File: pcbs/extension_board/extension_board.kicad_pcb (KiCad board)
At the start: 4 copper layers, 100 x 82.5 mm, 502 parts, among them J1 Conn_02x32_Counter_Clockwise, J2 Conn_02x03_Odd_Even, J3 Conn_01x05, J4 Conn_02x05_Odd_Even, J5 Barrel_Jack, J6 Conn_02x19_Odd_Even, J7 Conn_02x19_Odd_Even, J8 Conn_01x08, Q1 MBT3904DW1, Q10 MBT3904DW1, Q11 MBT3904DW1, Q12 MBT3904DW1, Q13 MBT3904DW1, Q14 MBT3904DW1, Q15 MBT3904DW1, Q16 MBT3904DW1, Q17 MBT3904DW1, Q18 MBT3904DW1, Q19 MBT3904DW1, Q2 MBT3904DW1, Q20 MBT3904DW1, Q21 MBT3904DW1, Q22 MBT3904DW1, Q23 MBT3904DW1, Q24 MBT3904DW1, Q25 MBT3904DW1, Q26 MBT3904DW1, Q27 MBT3904DW1, Q28 MBT3904DW1, Q29 MBT3904DW1, Q3 MBT3904DW1, Q30 MBT3904DW1, Q31 MBT3904DW1, Q32 MBT3904DW1, Q4 MBT3904DW1, Q5 MBT3904DW1, Q6 MBT3904DW1, Q7 MBT3904DW1, Q8 MBT3904DW1, Q9 MBT3904DW1, SW1 MY_SW_Push_Dual, SW2 Rotary_Encoder, SW3 Rotary_Encoder, U1 LM324QT, U10 LM324QT, U11 LM324QT, U12 LM324QT, U13 LM324QT, U14 LM324QT, U15 LM324QT, U16 LM324QT, U17 LM324QT, U18 LM324QT, U19 LM324QT, U2 LM324QT, U20 LM324QT, U21 LM324QT, U22 LM324QT, U23 LM324QT, U24 LM324QT, U25 LM324QT, U26 LM324QT, U27 LM324QT, U28 LM324QT, U29 LM324QT, U3 LM324QT, U30 LM324QT, U31 LM324QT, U32 LM324QT, U33 DAC101C085, U34 TS30011/12/13, U4 LM324QT, U5 LM324QT, U6 LM324QT, U7 LM324QT, U8 LM324QT, U9 LM324QT

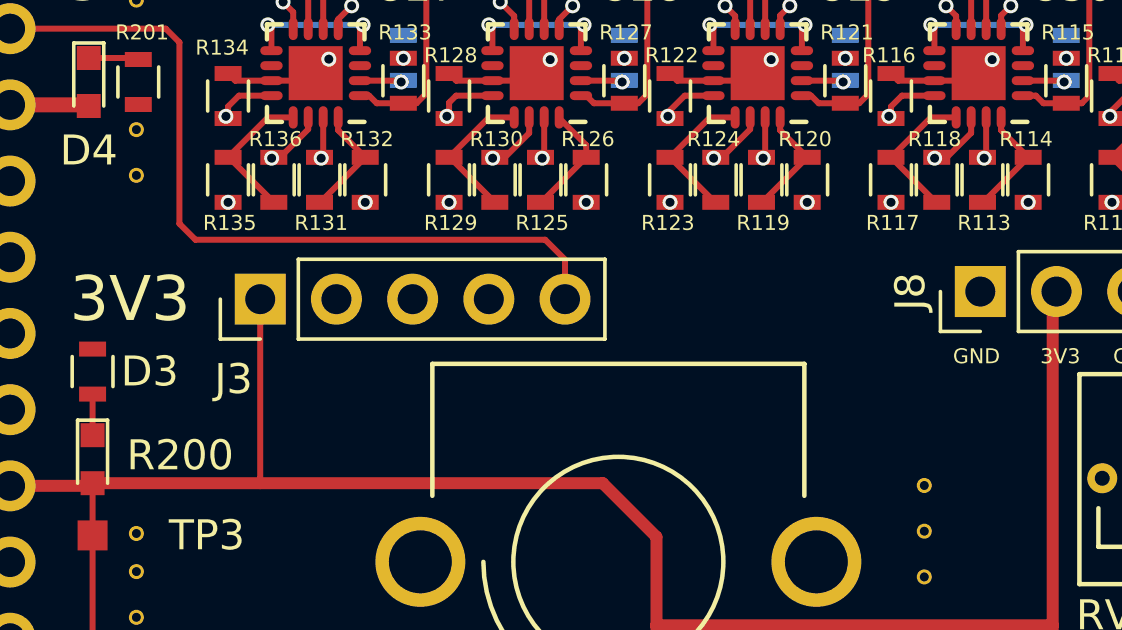
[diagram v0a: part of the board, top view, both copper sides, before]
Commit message: Added an adapter board (2 layers).
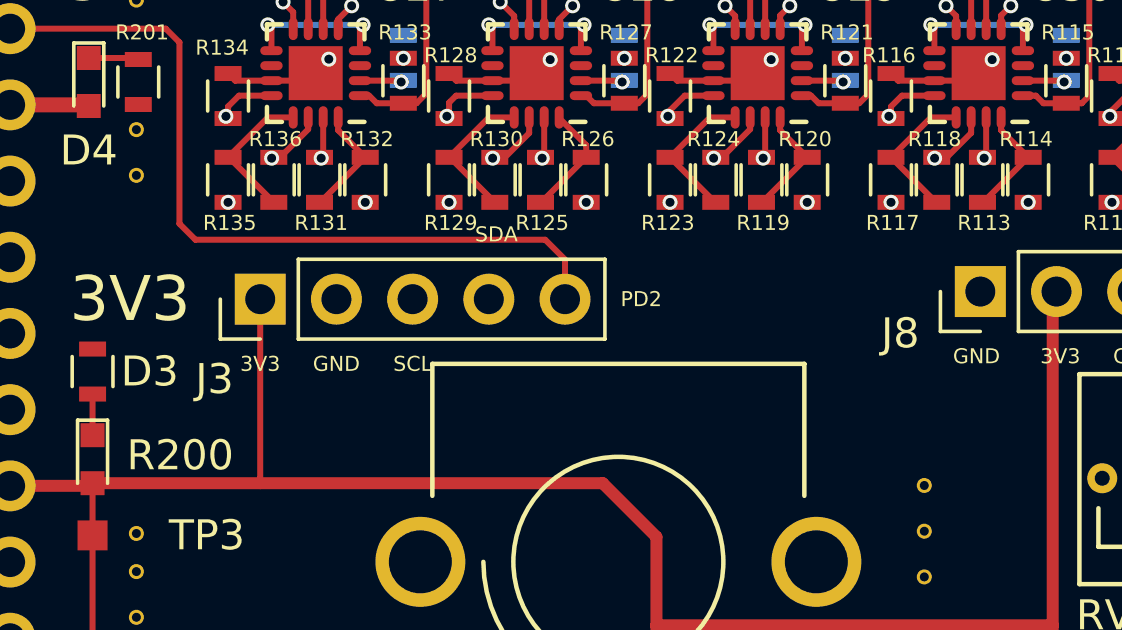
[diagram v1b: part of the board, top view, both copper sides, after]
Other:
- board text added: "PD2"
- board text added: "SCL"
- board text added: "SDA"
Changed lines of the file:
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@@
     (area 97.949999 46.949999 198.050001 129.550001)
     (thickness 1.6)
-    (drawings 38)
+    (drawings 44)
     (tracks 3807)
     (zones 0)
@@
     (38 B.Mask user)
     (39 F.Mask user)
-    (40 Dwgs.User user hide)
+    (40 Dwgs.User user)
     (41 Cmts.User user)
     (42 Eco1.User user)
@@
     (descr "Through hole straight pin header, 1x05, 2.54mm pitch, single row")
     (tags "Through hole pin header THT 1x05 2.54mm single row")
-    (fp_text reference J3 (at -2.667 -0.889 180) (layer F.SilkS)
+    (fp_text reference J3 (at -2.667 -1.524 180) (layer F.SilkS)
       (effects (font (size 1 1) (thickness 0.15)))
     )
@@
     (descr "Through hole straight pin header, 1x08, 2.54mm pitch, single row")
     (tags "Through hole pin header THT 1x08 2.54mm single row")
-    (fp_text reference J8 (at 0 -2.33 90) (layer F.SilkS)
+    (fp_text reference J8 (at -1.397 -2.667 180) (layer F.SilkS)
       (effects (font (size 1 1) (thickness 0.15)))
     )
@@
       (net 355 PA6))
   )
+  (gr_text PD2 (at 139.827 90.297) (layer F.SilkS)
+    (effects (font (size 0.5 0.5) (thickness 0.125)))
+  )
+  (gr_text SDA (at 135.001 88.138) (layer F.SilkS)
+    (effects (font (size 0.5 0.5) (thickness 0.125)))
+  )
+  (gr_text SCL (at 132.207 92.456) (layer F.SilkS)
+    (effects (font (size 0.5 0.5) (thickness 0.125)))
+  )
+  (gr_text GND (at 129.667 92.456) (layer F.SilkS)
+    (effects (font (size 0.5 0.5) (thickness 0.125)))
+  )
+  (gr_text 3V3 (at 127.127 92.456) (layer F.SilkS)
+    (effects (font (size 0.5 0.5) (thickness 0.125)))
+  )
+  (dimension 3 (width 0.3) (layer Dwgs.User)
+    (gr_text "3,000 mm" (at 184.5 128 270) (layer Dwgs.User)
+      (effects (font (size 1.5 1.5) (thickness 0.3)))
+    )
+    (feature1 (pts (xy 183 129.5) (xy 178.8 129.5)))
+    (feature2 (pts (xy 183 126.5) (xy 178.8 126.5)))
+    (crossbar (pts (xy 181.5 126.5) (xy 181.5 129.5)))
+    (arrow1a (pts (xy 181.5 129.5) (xy 180.913579 128.373496)))
+    (arrow1b (pts (xy 181.5 129.5) (xy 182.086421 128.373496)))
+    (arrow2a (pts (xy 181.5 126.5) (xy 180.913579 127.626504)))
+    (arrow2b (pts (xy 181.5 126.5) (xy 182.086421 127.626504)))
+  )
   (gr_text MISO (at 168.91 87.884) (layer F.SilkS)

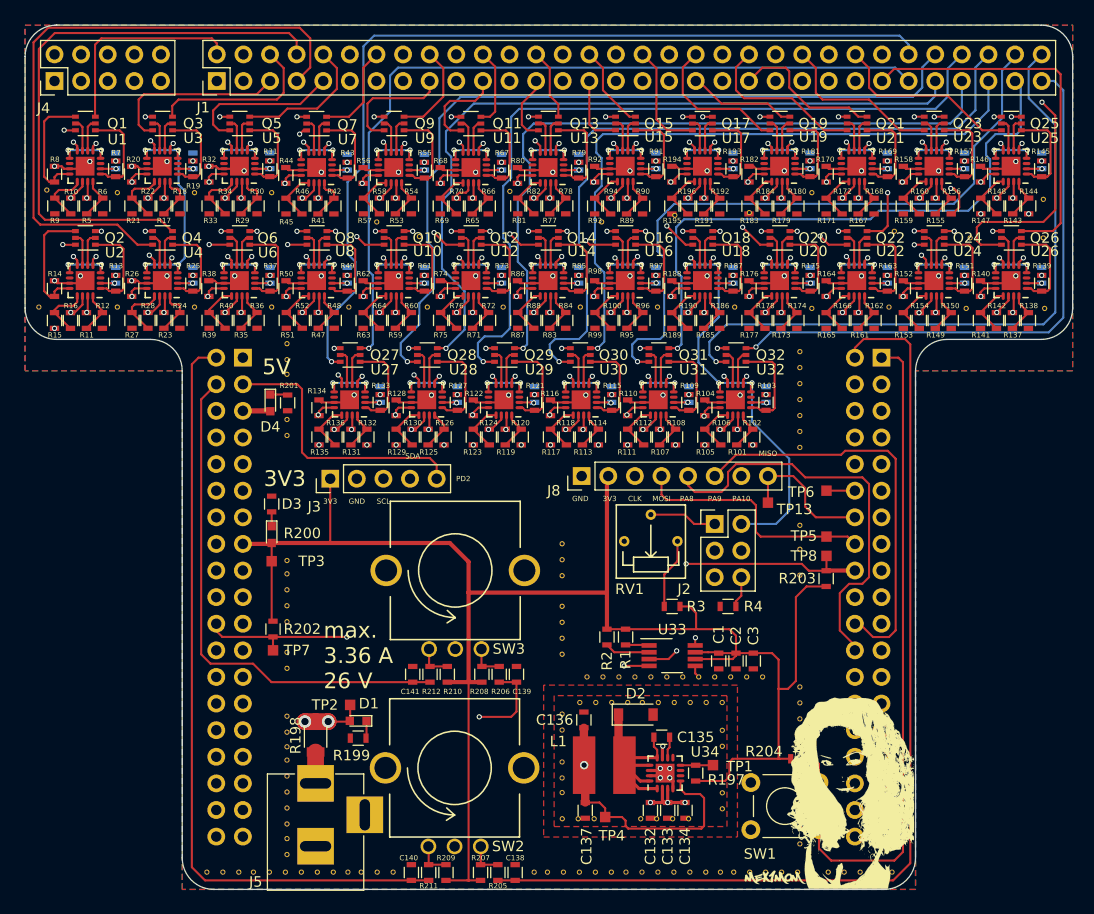
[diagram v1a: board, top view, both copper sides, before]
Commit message: Changed transistor array of driver for SOT-23 discrete transistor (more dissipation allowed).
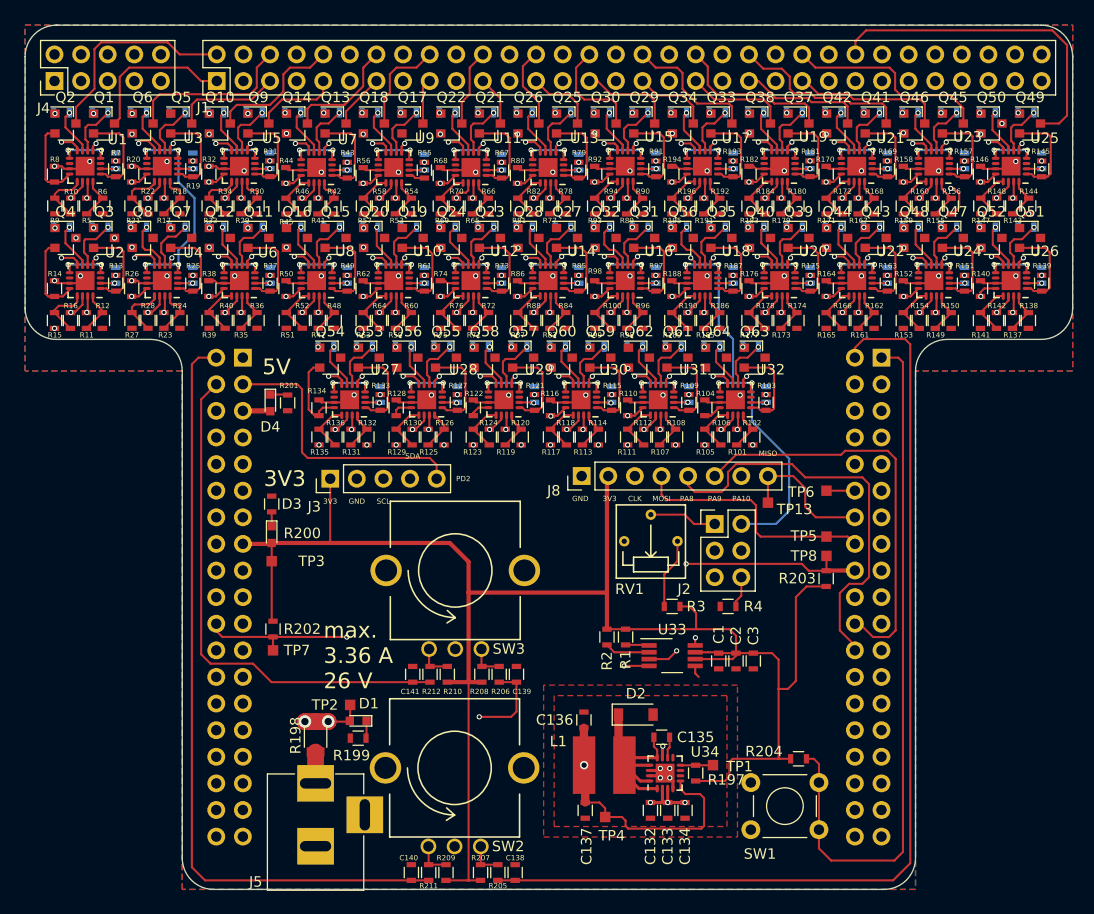
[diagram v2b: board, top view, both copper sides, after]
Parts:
- removed G***: LOGO, MyPics:logog1
- removed REF** (x152): Stitching-Via-0.3-0.5, MyVias:Stitchging-Via-0.3-0.5
- added Q33: MMBT3904, TO_SOT_Packages_SMD:SOT-23, F.Cu at (164.5, 56.4)
- added Q34: MMBT3904, TO_SOT_Packages_SMD:SOT-23, F.Cu at (160.8, 56.4)
- added Q35: MMBT3904, TO_SOT_Packages_SMD:SOT-23, F.Cu at (164.5, 67.3)
- added Q36: MMBT3904, TO_SOT_Packages_SMD:SOT-23, F.Cu at (160.8, 67.3)
- added Q37: MMBT3904, TO_SOT_Packages_SMD:SOT-23, F.Cu at (171.8, 56.4)
- added Q38: MMBT3904, TO_SOT_Packages_SMD:SOT-23, F.Cu at (168.1, 56.4)
- added Q39: MMBT3904, TO_SOT_Packages_SMD:SOT-23, F.Cu at (171.8, 67.3)
- added Q40: MMBT3904, TO_SOT_Packages_SMD:SOT-23, F.Cu at (168.1, 67.3)
- added Q41: MMBT3904, TO_SOT_Packages_SMD:SOT-23, F.Cu at (179.2, 56.4)
- added Q42: MMBT3904, TO_SOT_Packages_SMD:SOT-23, F.Cu at (175.5, 56.4)
- added Q43: MMBT3904, TO_SOT_Packages_SMD:SOT-23, F.Cu at (179.2, 67.3)
- added Q44: MMBT3904, TO_SOT_Packages_SMD:SOT-23, F.Cu at (175.5, 67.3)
- added Q45: MMBT3904, TO_SOT_Packages_SMD:SOT-23, F.Cu at (186.6, 56.4)
- added Q46: MMBT3904, TO_SOT_Packages_SMD:SOT-23, F.Cu at (182.9, 56.4)
- added Q47: MMBT3904, TO_SOT_Packages_SMD:SOT-23, F.Cu at (186.6, 67.3)
- added Q48: MMBT3904, TO_SOT_Packages_SMD:SOT-23, F.Cu at (182.9, 67.3)
- added Q49: MMBT3904, TO_SOT_Packages_SMD:SOT-23, F.Cu at (193.9, 56.4)
- added Q50: MMBT3904, TO_SOT_Packages_SMD:SOT-23, F.Cu at (190.2, 56.4)
- added Q51: MMBT3904, TO_SOT_Packages_SMD:SOT-23, F.Cu at (193.9, 67.3)
- added Q52: MMBT3904, TO_SOT_Packages_SMD:SOT-23, F.Cu at (190.2, 67.3)
- added Q53: MMBT3904, TO_SOT_Packages_SMD:SOT-23, F.Cu at (130.8, 78.7)
- added Q54: MMBT3904, TO_SOT_Packages_SMD:SOT-23, F.Cu at (127.1, 78.7)
- added Q55: MMBT3904, TO_SOT_Packages_SMD:SOT-23, F.Cu at (138.2, 78.7)
- added Q56: MMBT3904, TO_SOT_Packages_SMD:SOT-23, F.Cu at (134.5, 78.7)
- added Q57: MMBT3904, TO_SOT_Packages_SMD:SOT-23, F.Cu at (145.5, 78.7)
- added Q58: MMBT3904, TO_SOT_Packages_SMD:SOT-23, F.Cu at (141.9, 78.7)
- added Q59: MMBT3904, TO_SOT_Packages_SMD:SOT-23, F.Cu at (152.9, 78.7)
- added Q60: MMBT3904, TO_SOT_Packages_SMD:SOT-23, F.Cu at (149.2, 78.7)
- added Q61: MMBT3904, TO_SOT_Packages_SMD:SOT-23, F.Cu at (160.3, 78.7)
- added Q62: MMBT3904, TO_SOT_Packages_SMD:SOT-23, F.Cu at (156.6, 78.7)
- added Q63: MMBT3904, TO_SOT_Packages_SMD:SOT-23, F.Cu at (167.6, 78.7)
- added Q64: MMBT3904, TO_SOT_Packages_SMD:SOT-23, F.Cu at (164.0, 78.7)
- added R213: 10k, Resistors_SMD:R_0603, B.Cu at (105.2, 55.4)
- added R214: 10k, Resistors_SMD:R_0603, B.Cu at (101.5, 55.4)
- added R215: 10k, Resistors_SMD:R_0603, B.Cu at (105.2, 66.3)
- added R216: 10k, Resistors_SMD:R_0603, B.Cu at (101.5, 66.3)
- added R217: 10k, Resistors_SMD:R_0603, B.Cu at (112.5, 55.4)
- added R218: 10k, Resistors_SMD:R_0603, B.Cu at (108.8, 55.4)
- added R219: 10k, Resistors_SMD:R_0603, B.Cu at (112.5, 66.3)
- added R220: 10k, Resistors_SMD:R_0603, B.Cu at (108.8, 66.3)
- added R221: 10k, Resistors_SMD:R_0603, B.Cu at (119.9, 55.4)
- added R222: 10k, Resistors_SMD:R_0603, B.Cu at (116.2, 55.4)
- added R223: 10k, Resistors_SMD:R_0603, B.Cu at (119.9, 66.3)
- added R224: 10k, Resistors_SMD:R_0603, B.Cu at (116.2, 66.3)
- added R225: 10k, Resistors_SMD:R_0603, B.Cu at (127.3, 55.4)
- added R226: 10k, Resistors_SMD:R_0603, B.Cu at (123.6, 55.4)
- added R227: 10k, Resistors_SMD:R_0603, B.Cu at (127.3, 66.3)
- added R228: 10k, Resistors_SMD:R_0603, B.Cu at (123.6, 66.3)
- added R229: 10k, Resistors_SMD:R_0603, B.Cu at (134.6, 55.4)
- added R230: 10k, Resistors_SMD:R_0603, B.Cu at (130.9, 55.4)
- added R231: 10k, Resistors_SMD:R_0603, B.Cu at (134.6, 66.3)
- added R232: 10k, Resistors_SMD:R_0603, B.Cu at (130.9, 66.3)
- added R233: 10k, Resistors_SMD:R_0603, B.Cu at (142.0, 55.4)
- added R234: 10k, Resistors_SMD:R_0603, B.Cu at (138.3, 55.4)
- added R235: 10k, Resistors_SMD:R_0603, B.Cu at (142.0, 66.3)
- added R236: 10k, Resistors_SMD:R_0603, B.Cu at (138.3, 66.3)
- added R237: 10k, Resistors_SMD:R_0603, B.Cu at (149.4, 55.4)
- added R238: 10k, Resistors_SMD:R_0603, B.Cu at (145.7, 55.4)
- added R239: 10k, Resistors_SMD:R_0603, B.Cu at (149.4, 66.3)
- added R240: 10k, Resistors_SMD:R_0603, B.Cu at (145.7, 66.3)
- added R241: 10k, Resistors_SMD:R_0603, B.Cu at (156.7, 55.4)
- added R242: 10k, Resistors_SMD:R_0603, B.Cu at (153.0, 55.4)
- added R243: 10k, Resistors_SMD:R_0603, B.Cu at (156.7, 66.3)
- added R244: 10k, Resistors_SMD:R_0603, B.Cu at (153.0, 66.3)
- added R245: 10k, Resistors_SMD:R_0603, B.Cu at (167.3, 77.7)
- added R246: 10k, Resistors_SMD:R_0603, B.Cu at (163.6, 77.7)
- added R247: 10k, Resistors_SMD:R_0603, B.Cu at (159.9, 77.7)
- added R248: 10k, Resistors_SMD:R_0603, B.Cu at (156.2, 77.7)
- added R249: 10k, Resistors_SMD:R_0603, B.Cu at (152.5, 77.7)
- added R250: 10k, Resistors_SMD:R_0603, B.Cu at (148.8, 77.7)
- added R251: 10k, Resistors_SMD:R_0603, B.Cu at (145.2, 77.7)
- added R252: 10k, Resistors_SMD:R_0603, B.Cu at (141.5, 77.7)
- added R253: 10k, Resistors_SMD:R_0603, B.Cu at (137.8, 77.7)
- added R254: 10k, Resistors_SMD:R_0603, B.Cu at (134.1, 77.7)
- added R255: 10k, Resistors_SMD:R_0603, B.Cu at (130.4, 77.7)
- added R256: 10k, Resistors_SMD:R_0603, B.Cu at (126.7, 77.7)
- added R257: 10k, Resistors_SMD:R_0603, B.Cu at (193.5, 66.3)
- added R258: 10k, Resistors_SMD:R_0603, B.Cu at (189.9, 66.3)
- added R259: 10k, Resistors_SMD:R_0603, B.Cu at (193.5, 55.4)
- added R260: 10k, Resistors_SMD:R_0603, B.Cu at (189.9, 55.4)
- added R261: 10k, Resistors_SMD:R_0603, B.Cu at (186.2, 66.3)
- added R262: 10k, Resistors_SMD:R_0603, B.Cu at (182.5, 66.3)
- added R263: 10k, Resistors_SMD:R_0603, B.Cu at (186.2, 55.4)
- added R264: 10k, Resistors_SMD:R_0603, B.Cu at (182.5, 55.4)
- added R265: 10k, Resistors_SMD:R_0603, B.Cu at (178.8, 66.3)
- added R266: 10k, Resistors_SMD:R_0603, B.Cu at (175.1, 66.3)
- added R267: 10k, Resistors_SMD:R_0603, B.Cu at (178.8, 55.4)
- added R268: 10k, Resistors_SMD:R_0603, B.Cu at (175.1, 55.4)
- added R269: 10k, Resistors_SMD:R_0603, B.Cu at (171.4, 66.3)
- added R270: 10k, Resistors_SMD:R_0603, B.Cu at (167.8, 66.3)
- added R271: 10k, Resistors_SMD:R_0603, B.Cu at (171.4, 55.4)
- added R272: 10k, Resistors_SMD:R_0603, B.Cu at (167.8, 55.4)
- added R273: 10k, Resistors_SMD:R_0603, B.Cu at (164.1, 66.3)
- added R274: 10k, Resistors_SMD:R_0603, B.Cu at (160.4, 66.3)
- added R275: 10k, Resistors_SMD:R_0603, B.Cu at (164.1, 55.4)
- added R276: 10k, Resistors_SMD:R_0603, B.Cu at (160.4, 55.4)
- Q1, Q10, Q11, Q12, Q13, Q14, Q15, Q16, Q17, Q18, Q19, Q2, Q20, Q21, Q22, Q23, Q24, Q25, Q26, Q27, Q28, Q29, Q3, Q30, Q31, Q32, Q4, Q5, Q6, Q7, Q8, Q9: value MBT3904DW1 -> MMBT3904; footprint TO_SOT_Packages_SMD:SOT-363_SC-70-6 -> TO_SOT_Packages_SMD:SOT-23
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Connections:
- Q1 pad 3: LED_N_02 -> LED_N_01
- Q10 pad 3: LED_N_20 -> LED_N_10
- Q11 pad 3: LED_N_22 -> LED_N_11
- Q12 pad 3: LED_N_24 -> LED_N_12
- Q13 pad 3: LED_N_26 -> LED_N_13
- Q14 pad 3: LED_N_28 -> LED_N_14
- Q15 pad 3: LED_N_30 -> LED_N_15
- Q16 pad 3: LED_N_32 -> LED_N_16
- Q17 pad 3: LED_N_33 -> LED_N_17
- Q18 pad 3: LED_N_35 -> LED_N_18
- Q19 pad 3: LED_N_37 -> LED_N_19
- Q2 pad 3: LED_N_04 -> LED_N_02
- Q20 pad 3: LED_N_39 -> LED_N_20
- Q21 pad 3: LED_N_41 -> LED_N_21
- Q22 pad 3: LED_N_43 -> LED_N_22
- Q23 pad 3: LED_N_45 -> LED_N_23
- Q24 pad 3: LED_N_47 -> LED_N_24
- Q25 pad 3: LED_N_49 -> LED_N_25
- Q26 pad 3: LED_N_51 -> LED_N_26
- Q27 pad 3: LED_N_53 -> LED_N_27
- Q28 pad 3: LED_N_55 -> LED_N_28
- Q29 pad 3: LED_N_57 -> LED_N_29
- Q3 pad 3: LED_N_06 -> LED_N_03
- Q30 pad 3: LED_N_59 -> LED_N_30
- Q31 pad 3: LED_N_61 -> LED_N_31
- Q32 pad 3: LED_N_63 -> LED_N_32
- Q4 pad 3: LED_N_08 -> LED_N_04
- Q5 pad 3: LED_N_10 -> LED_N_05
- Q6 pad 3: LED_N_12 -> LED_N_06
- Q7 pad 3: LED_N_14 -> LED_N_07
- Q8 pad 3: LED_N_16 -> LED_N_08
- Q9 pad 3: LED_N_18 -> LED_N_09
- R103 pad 1: Net-(Q32-Pad1) -> Net-(Q63-Pad2)
- R104 pad 1: Net-(Q32-Pad4) -> Net-(Q64-Pad2)
- R109 pad 1: Net-(Q31-Pad1) -> Net-(Q61-Pad2)
- R110 pad 1: Net-(Q31-Pad4) -> Net-(Q62-Pad2)
- R115 pad 1: Net-(Q30-Pad1) -> Net-(Q59-Pad2)
- R116 pad 1: Net-(Q30-Pad4) -> Net-(Q60-Pad2)
- R121 pad 1: Net-(Q29-Pad1) -> Net-(Q57-Pad2)
- R122 pad 1: Net-(Q29-Pad4) -> Net-(Q58-Pad2)
- R127 pad 1: Net-(Q28-Pad1) -> Net-(Q55-Pad2)
- R128 pad 1: Net-(Q28-Pad4) -> Net-(Q56-Pad2)
- R13 pad 1: Net-(Q2-Pad1) -> Net-(Q3-Pad2)
- R133 pad 1: Net-(Q27-Pad1) -> Net-(Q53-Pad2)
- R134 pad 1: Net-(Q27-Pad4) -> Net-(Q54-Pad2)
- R139 pad 1: Net-(Q26-Pad1) -> Net-(Q51-Pad2)
- R14 pad 1: Net-(Q2-Pad4) -> Net-(Q4-Pad2)
- R140 pad 1: Net-(Q26-Pad4) -> Net-(Q52-Pad2)
- R145 pad 1: Net-(Q25-Pad1) -> Net-(Q49-Pad2)
- R146 pad 1: Net-(Q25-Pad4) -> Net-(Q50-Pad2)
- R151 pad 1: Net-(Q24-Pad1) -> Net-(Q47-Pad2)
- R152 pad 1: Net-(Q24-Pad4) -> Net-(Q48-Pad2)
- R157 pad 1: Net-(Q23-Pad1) -> Net-(Q45-Pad2)
- R158 pad 1: Net-(Q23-Pad4) -> Net-(Q46-Pad2)
- R163 pad 1: Net-(Q22-Pad1) -> Net-(Q43-Pad2)
- R164 pad 1: Net-(Q22-Pad4) -> Net-(Q44-Pad2)
- R169 pad 1: Net-(Q21-Pad1) -> Net-(Q41-Pad2)
- R170 pad 1: Net-(Q21-Pad4) -> Net-(Q42-Pad2)
- R175 pad 1: Net-(Q20-Pad1) -> Net-(Q39-Pad2)
- R176 pad 1: Net-(Q20-Pad4) -> Net-(Q40-Pad2)
- R181 pad 1: Net-(Q19-Pad1) -> Net-(Q37-Pad2)
- R182 pad 1: Net-(Q19-Pad4) -> Net-(Q38-Pad2)
- R187 pad 1: Net-(Q18-Pad1) -> Net-(Q35-Pad2)
- R188 pad 1: Net-(Q18-Pad4) -> Net-(Q36-Pad2)
- R19 pad 1: Net-(Q3-Pad1) -> Net-(Q5-Pad2)
- R193 pad 1: Net-(Q17-Pad1) -> Net-(Q33-Pad2)
- R194 pad 1: Net-(Q17-Pad4) -> Net-(Q34-Pad2)
- R20 pad 1: Net-(Q3-Pad4) -> Net-(Q6-Pad2)
- R25 pad 1: Net-(Q4-Pad1) -> Net-(Q7-Pad2)
- R26 pad 1: Net-(Q4-Pad4) -> Net-(Q8-Pad2)
- R31 pad 1: Net-(Q5-Pad1) -> Net-(Q9-Pad2)
- R32 pad 1: Net-(Q5-Pad4) -> Net-(Q10-Pad2)
- R37 pad 1: Net-(Q6-Pad1) -> Net-(Q11-Pad2)
- R38 pad 1: Net-(Q6-Pad4) -> Net-(Q12-Pad2)
- R43 pad 1: Net-(Q7-Pad1) -> Net-(Q13-Pad2)
- R44 pad 1: Net-(Q7-Pad4) -> Net-(Q14-Pad2)
- R49 pad 1: Net-(Q8-Pad1) -> Net-(Q15-Pad2)
- R50 pad 1: Net-(Q8-Pad4) -> Net-(Q16-Pad2)
- R55 pad 1: Net-(Q9-Pad1) -> Net-(Q17-Pad2)
- R56 pad 1: Net-(Q9-Pad4) -> Net-(Q18-Pad2)
- R61 pad 1: Net-(Q10-Pad1) -> Net-(Q19-Pad2)
- R62 pad 1: Net-(Q10-Pad4) -> Net-(Q20-Pad2)
- R67 pad 1: Net-(Q11-Pad1) -> Net-(Q21-Pad2)
- R68 pad 1: Net-(Q11-Pad4) -> Net-(Q22-Pad2)
- R7 pad 1: Net-(Q1-Pad1) -> Net-(Q1-Pad2)
- R73 pad 1: Net-(Q12-Pad1) -> Net-(Q23-Pad2)
- R74 pad 1: Net-(Q12-Pad4) -> Net-(Q24-Pad2)
- R79 pad 1: Net-(Q13-Pad1) -> Net-(Q25-Pad2)
- R8 pad 1: Net-(Q1-Pad4) -> Net-(Q2-Pad2)
- R80 pad 1: Net-(Q13-Pad4) -> Net-(Q26-Pad2)
- R85 pad 1: Net-(Q14-Pad1) -> Net-(Q27-Pad2)
- R86 pad 1: Net-(Q14-Pad4) -> Net-(Q28-Pad2)
- R91 pad 1: Net-(Q15-Pad1) -> Net-(Q29-Pad2)
- R92 pad 1: Net-(Q15-Pad4) -> Net-(Q30-Pad2)
- R97 pad 1: Net-(Q16-Pad1) -> Net-(Q31-Pad2)
- R98 pad 1: Net-(Q16-Pad4) -> Net-(Q32-Pad2)
- U1 pad 1: Net-(Q1-Pad1) -> Net-(Q1-Pad2)
- U1 pad 12: Net-(Q1-Pad4) -> Net-(Q2-Pad2)
- U1 pad 17: GND -> (no net)
- U1 pad 6: Net-(Q1-Pad2) -> Net-(R213-Pad2)
- U1 pad 7: Net-(Q1-Pad5) -> Net-(R214-Pad1)
- U10 pad 1: Net-(Q10-Pad1) -> Net-(Q19-Pad2)
- U10 pad 12: Net-(Q10-Pad4) -> Net-(Q20-Pad2)
- U10 pad 17: GND -> (no net)
- U10 pad 6: Net-(Q10-Pad2) -> Net-(R231-Pad2)
- U10 pad 7: Net-(Q10-Pad5) -> Net-(R232-Pad1)
- U11 pad 1: Net-(Q11-Pad1) -> Net-(Q21-Pad2)
- U11 pad 12: Net-(Q11-Pad4) -> Net-(Q22-Pad2)
- U11 pad 17: GND -> (no net)
- U11 pad 6: Net-(Q11-Pad2) -> Net-(R233-Pad2)
- U11 pad 7: Net-(Q11-Pad5) -> Net-(R234-Pad1)
- U12 pad 1: Net-(Q12-Pad1) -> Net-(Q23-Pad2)
- U12 pad 12: Net-(Q12-Pad4) -> Net-(Q24-Pad2)
- U12 pad 17: GND -> (no net)
- U12 pad 6: Net-(Q12-Pad2) -> Net-(R235-Pad2)
- U12 pad 7: Net-(Q12-Pad5) -> Net-(R236-Pad1)
- U13 pad 1: Net-(Q13-Pad1) -> Net-(Q25-Pad2)
- U13 pad 12: Net-(Q13-Pad4) -> Net-(Q26-Pad2)
- U13 pad 17: GND -> (no net)
- U13 pad 6: Net-(Q13-Pad2) -> Net-(R237-Pad2)
- U13 pad 7: Net-(Q13-Pad5) -> Net-(R238-Pad1)
- U14 pad 1: Net-(Q14-Pad1) -> Net-(Q27-Pad2)
- U14 pad 12: Net-(Q14-Pad4) -> Net-(Q28-Pad2)
- U14 pad 17: GND -> (no net)
- U14 pad 6: Net-(Q14-Pad2) -> Net-(R239-Pad2)
- U14 pad 7: Net-(Q14-Pad5) -> Net-(R240-Pad1)
- U15 pad 1: Net-(Q15-Pad1) -> Net-(Q29-Pad2)
- U15 pad 12: Net-(Q15-Pad4) -> Net-(Q30-Pad2)
- U15 pad 17: GND -> (no net)
- U15 pad 6: Net-(Q15-Pad2) -> Net-(R241-Pad2)
- U15 pad 7: Net-(Q15-Pad5) -> Net-(R242-Pad1)
- U16 pad 1: Net-(Q16-Pad1) -> Net-(Q31-Pad2)
- U16 pad 12: Net-(Q16-Pad4) -> Net-(Q32-Pad2)
- U16 pad 17: GND -> (no net)
- U16 pad 6: Net-(Q16-Pad2) -> Net-(R243-Pad2)
- U16 pad 7: Net-(Q16-Pad5) -> Net-(R244-Pad1)
- U17 pad 1: Net-(Q17-Pad1) -> Net-(Q33-Pad2)
- U17 pad 12: Net-(Q17-Pad4) -> Net-(Q34-Pad2)
- U17 pad 17: GND -> (no net)
- U17 pad 6: Net-(Q17-Pad2) -> Net-(R275-Pad2)
- U17 pad 7: Net-(Q17-Pad5) -> Net-(R276-Pad1)
- U18 pad 1: Net-(Q18-Pad1) -> Net-(Q35-Pad2)
- U18 pad 12: Net-(Q18-Pad4) -> Net-(Q36-Pad2)
- U18 pad 17: GND -> (no net)
- U18 pad 6: Net-(Q18-Pad2) -> Net-(R273-Pad2)
- U18 pad 7: Net-(Q18-Pad5) -> Net-(R274-Pad1)
- U19 pad 1: Net-(Q19-Pad1) -> Net-(Q37-Pad2)
- U19 pad 12: Net-(Q19-Pad4) -> Net-(Q38-Pad2)
- U19 pad 17: GND -> (no net)
- U19 pad 6: Net-(Q19-Pad2) -> Net-(R271-Pad2)
- U19 pad 7: Net-(Q19-Pad5) -> Net-(R272-Pad1)
- U2 pad 1: Net-(Q2-Pad1) -> Net-(Q3-Pad2)
- U2 pad 12: Net-(Q2-Pad4) -> Net-(Q4-Pad2)
- U2 pad 17: GND -> (no net)
- U2 pad 6: Net-(Q2-Pad2) -> Net-(R215-Pad2)
- U2 pad 7: Net-(Q2-Pad5) -> Net-(R216-Pad1)
- U20 pad 1: Net-(Q20-Pad1) -> Net-(Q39-Pad2)
- U20 pad 12: Net-(Q20-Pad4) -> Net-(Q40-Pad2)
- U20 pad 17: GND -> (no net)
- U20 pad 6: Net-(Q20-Pad2) -> Net-(R269-Pad2)
- U20 pad 7: Net-(Q20-Pad5) -> Net-(R270-Pad1)
- U21 pad 1: Net-(Q21-Pad1) -> Net-(Q41-Pad2)
- U21 pad 12: Net-(Q21-Pad4) -> Net-(Q42-Pad2)
- U21 pad 17: GND -> (no net)
- U21 pad 6: Net-(Q21-Pad2) -> Net-(R267-Pad2)
- U21 pad 7: Net-(Q21-Pad5) -> Net-(R268-Pad1)
- U22 pad 1: Net-(Q22-Pad1) -> Net-(Q43-Pad2)
- U22 pad 12: Net-(Q22-Pad4) -> Net-(Q44-Pad2)
- U22 pad 17: GND -> (no net)
- U22 pad 6: Net-(Q22-Pad2) -> Net-(R265-Pad2)
- U22 pad 7: Net-(Q22-Pad5) -> Net-(R266-Pad1)
- U23 pad 1: Net-(Q23-Pad1) -> Net-(Q45-Pad2)
- U23 pad 12: Net-(Q23-Pad4) -> Net-(Q46-Pad2)
- U23 pad 17: GND -> (no net)
- U23 pad 6: Net-(Q23-Pad2) -> Net-(R263-Pad2)
- U23 pad 7: Net-(Q23-Pad5) -> Net-(R264-Pad1)
- U24 pad 1: Net-(Q24-Pad1) -> Net-(Q47-Pad2)
- U24 pad 12: Net-(Q24-Pad4) -> Net-(Q48-Pad2)
- U24 pad 17: GND -> (no net)
- U24 pad 6: Net-(Q24-Pad2) -> Net-(R261-Pad2)
- U24 pad 7: Net-(Q24-Pad5) -> Net-(R262-Pad1)
- U25 pad 1: Net-(Q25-Pad1) -> Net-(Q49-Pad2)
- U25 pad 12: Net-(Q25-Pad4) -> Net-(Q50-Pad2)
- U25 pad 17: GND -> (no net)
- U25 pad 6: Net-(Q25-Pad2) -> Net-(R259-Pad2)
- U25 pad 7: Net-(Q25-Pad5) -> Net-(R260-Pad1)
- U26 pad 1: Net-(Q26-Pad1) -> Net-(Q51-Pad2)
- U26 pad 12: Net-(Q26-Pad4) -> Net-(Q52-Pad2)
- U26 pad 17: GND -> (no net)
- U26 pad 6: Net-(Q26-Pad2) -> Net-(R257-Pad2)
- U26 pad 7: Net-(Q26-Pad5) -> Net-(R258-Pad1)
- U27 pad 1: Net-(Q27-Pad1) -> Net-(Q53-Pad2)
- U27 pad 12: Net-(Q27-Pad4) -> Net-(Q54-Pad2)
- U27 pad 17: GND -> (no net)
- U27 pad 6: Net-(Q27-Pad2) -> Net-(R255-Pad2)
- U27 pad 7: Net-(Q27-Pad5) -> Net-(R256-Pad1)
- U28 pad 1: Net-(Q28-Pad1) -> Net-(Q55-Pad2)
- U28 pad 12: Net-(Q28-Pad4) -> Net-(Q56-Pad2)
- U28 pad 17: GND -> (no net)
- U28 pad 6: Net-(Q28-Pad2) -> Net-(R253-Pad2)
- U28 pad 7: Net-(Q28-Pad5) -> Net-(R254-Pad1)
- U29 pad 1: Net-(Q29-Pad1) -> Net-(Q57-Pad2)
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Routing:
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
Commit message: Produced Gerber files for both boards. Ready for production.
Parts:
- added G***: LOGO, MyPics:esd, F.Cu at (150.4, 99.7)
- added G***: LOGO, MyPics:logog1, F.Cu at (174.8, 120.1)
- added REF**: Stitching-Via-0.3-0.5, MyVias:Stitchging-Via-0.3-0.5, F.Cu at (124.9, 103.6)
- added REF**: Stitching-Via-0.3-0.5, MyVias:Stitchging-Via-0.3-0.5, F.Cu at (119.3, 128.0)
- added REF**: Stitching-Via-0.3-0.5, MyVias:Stitchging-Via-0.3-0.5, F.Cu at (161.1, 123.1)
- added REF**: Stitching-Via-0.3-0.5, MyVias:Stitchging-Via-0.3-0.5, F.Cu at (162.1, 123.1)
- added REF**: Stitching-Via-0.3-0.5, MyVias:Stitchging-Via-0.3-0.5, F.Cu at (162.1, 111.4)
- added REF**: Stitching-Via-0.3-0.5, MyVias:Stitchging-Via-0.3-0.5, F.Cu at (163.1, 111.4)
- added REF**: Stitching-Via-0.3-0.5, MyVias:Stitchging-Via-0.3-0.5, F.Cu at (161.1, 111.4)
- added REF**: Stitching-Via-0.3-0.5, MyVias:Stitchging-Via-0.3-0.5, F.Cu at (164.2, 111.4)
- added REF**: Stitching-Via-0.3-0.5, MyVias:Stitchging-Via-0.3-0.5, F.Cu at (156.0, 111.4)
- added REF**: Stitching-Via-0.3-0.5, MyVias:Stitchging-Via-0.3-0.5, F.Cu at (157.0, 111.4)
- added REF**: Stitching-Via-0.3-0.5, MyVias:Stitchging-Via-0.3-0.5, F.Cu at (155.0, 111.4)
- added REF**: Stitching-Via-0.3-0.5, MyVias:Stitchging-Via-0.3-0.5, F.Cu at (158.1, 111.4)
- added REF**: Stitching-Via-0.3-0.5, MyVias:Stitchging-Via-0.3-0.5, F.Cu at (121.1, 128.0)
- added REF**: Stitching-Via-0.3-0.5, MyVias:Stitchging-Via-0.3-0.5, F.Cu at (160.1, 111.4)
- added REF**: Stitching-Via-0.3-0.5, MyVias:Stitchging-Via-0.3-0.5, F.Cu at (159.1, 111.4)
- added REF**: Stitching-Via-0.3-0.5, MyVias:Stitchging-Via-0.3-0.5, F.Cu at (153.0, 111.4)
- added REF**: Stitching-Via-0.3-0.5, MyVias:Stitchging-Via-0.3-0.5, F.Cu at (154.0, 111.4)
- added REF**: Stitching-Via-0.3-0.5, MyVias:Stitchging-Via-0.3-0.5, F.Cu at (152.0, 111.4)
- added REF**: Stitching-Via-0.3-0.5, MyVias:Stitchging-Via-0.3-0.5, F.Cu at (151.0, 111.4)
- added REF**: Stitching-Via-0.3-0.5, MyVias:Stitchging-Via-0.3-0.5, F.Cu at (149.9, 111.4)
- added REF**: Stitching-Via-0.3-0.5, MyVias:Stitchging-Via-0.3-0.5, F.Cu at (149.0, 112.5)
- added REF**: Stitching-Via-0.3-0.5, MyVias:Stitchging-Via-0.3-0.5, F.Cu at (149.0, 113.5)
- added REF**: Stitching-Via-0.3-0.5, MyVias:Stitchging-Via-0.3-0.5, F.Cu at (149.0, 116.6)
- added REF**: Stitching-Via-0.3-0.5, MyVias:Stitchging-Via-0.3-0.5, F.Cu at (128.7, 128.0)
- added REF**: Stitching-Via-0.3-0.5, MyVias:Stitchging-Via-0.3-0.5, F.Cu at (149.0, 121.7)
- added REF**: Stitching-Via-0.3-0.5, MyVias:Stitchging-Via-0.3-0.5, F.Cu at (149.0, 120.7)
- added REF**: Stitching-Via-0.3-0.5, MyVias:Stitchging-Via-0.3-0.5, F.Cu at (149.0, 117.6)
- added REF**: Stitching-Via-0.3-0.5, MyVias:Stitchging-Via-0.3-0.5, F.Cu at (149.0, 119.6)
- added REF**: Stitching-Via-0.3-0.5, MyVias:Stitchging-Via-0.3-0.5, F.Cu at (149.0, 118.6)
- added REF**: Stitching-Via-0.3-0.5, MyVias:Stitchging-Via-0.3-0.5, F.Cu at (172.9, 73.4)
- added REF**: Stitching-Via-0.3-0.5, MyVias:Stitchging-Via-0.3-0.5, F.Cu at (172.9, 75.7)
- added REF**: Stitching-Via-0.3-0.5, MyVias:Stitchging-Via-0.3-0.5, F.Cu at (180.3, 73.4)
- added REF**: Stitching-Via-0.3-0.5, MyVias:Stitchging-Via-0.3-0.5, F.Cu at (180.3, 75.7)
- added REF**: Stitching-Via-0.3-0.5, MyVias:Stitchging-Via-0.3-0.5, F.Cu at (187.9, 75.4)
- added REF**: Stitching-Via-0.3-0.5, MyVias:Stitchging-Via-0.3-0.5, F.Cu at (126.9, 128.0)
- added REF**: Stitching-Via-0.3-0.5, MyVias:Stitchging-Via-0.3-0.5, F.Cu at (187.9, 73.4)
- added REF**: Stitching-Via-0.3-0.5, MyVias:Stitchging-Via-0.3-0.5, F.Cu at (195.3, 75.4)
- added REF**: Stitching-Via-0.3-0.5, MyVias:Stitchging-Via-0.3-0.5, F.Cu at (195.3, 73.4)
- added REF**: Stitching-Via-0.3-0.5, MyVias:Stitchging-Via-0.3-0.5, F.Cu at (195.3, 63.0)
- added REF**: Stitching-Via-0.3-0.5, MyVias:Stitchging-Via-0.3-0.5, F.Cu at (195.3, 64.8)
- added REF**: Stitching-Via-0.3-0.5, MyVias:Stitchging-Via-0.3-0.5, F.Cu at (163.3, 60.5)
- added REF**: Stitching-Via-0.3-0.5, MyVias:Stitchging-Via-0.3-0.5, F.Cu at (155.9, 60.5)
- added REF**: Stitching-Via-0.3-0.5, MyVias:Stitchging-Via-0.3-0.5, F.Cu at (187.9, 63.0)
- added REF**: Stitching-Via-0.3-0.5, MyVias:Stitchging-Via-0.3-0.5, F.Cu at (187.9, 64.8)
- added REF**: Stitching-Via-0.3-0.5, MyVias:Stitchging-Via-0.3-0.5, F.Cu at (180.5, 63.0)
- added REF**: Stitching-Via-0.3-0.5, MyVias:Stitchging-Via-0.3-0.5, F.Cu at (124.9, 128.0)
- added REF**: Stitching-Via-0.3-0.5, MyVias:Stitchging-Via-0.3-0.5, F.Cu at (180.5, 64.8)
- added REF**: Stitching-Via-0.3-0.5, MyVias:Stitchging-Via-0.3-0.5, F.Cu at (173.2, 63.0)
- added REF**: Stitching-Via-0.3-0.5, MyVias:Stitchging-Via-0.3-0.5, F.Cu at (173.2, 64.8)
- added REF**: Stitching-Via-0.3-0.5, MyVias:Stitchging-Via-0.3-0.5, F.Cu at (165.6, 63.8)
- added REF**: Stitching-Via-0.3-0.5, MyVias:Stitchging-Via-0.3-0.5, F.Cu at (165.6, 64.8)
- added REF**: Stitching-Via-0.3-0.5, MyVias:Stitchging-Via-0.3-0.5, F.Cu at (157.9, 65.0)
- added REF**: Stitching-Via-0.3-0.5, MyVias:Stitchging-Via-0.3-0.5, F.Cu at (157.9, 63.5)
- added REF**: Stitching-Via-0.3-0.5, MyVias:Stitchging-Via-0.3-0.5, F.Cu at (150.8, 63.0)
- added REF**: Stitching-Via-0.3-0.5, MyVias:Stitchging-Via-0.3-0.5, F.Cu at (150.8, 65.0)
- added REF**: Stitching-Via-0.3-0.5, MyVias:Stitchging-Via-0.3-0.5, F.Cu at (143.5, 63.0)
- added REF**: Stitching-Via-0.3-0.5, MyVias:Stitchging-Via-0.3-0.5, F.Cu at (122.9, 128.0)
- added REF**: Stitching-Via-0.3-0.5, MyVias:Stitchging-Via-0.3-0.5, F.Cu at (143.5, 65.0)
- added REF**: Stitching-Via-0.3-0.5, MyVias:Stitchging-Via-0.3-0.5, F.Cu at (136.1, 63.0)
- added REF**: Stitching-Via-0.3-0.5, MyVias:Stitchging-Via-0.3-0.5, F.Cu at (136.1, 65.0)
- added REF**: Stitching-Via-0.3-0.5, MyVias:Stitchging-Via-0.3-0.5, F.Cu at (128.7, 63.0)
- added REF**: Stitching-Via-0.3-0.5, MyVias:Stitchging-Via-0.3-0.5, F.Cu at (128.7, 65.0)
- added REF**: Stitching-Via-0.3-0.5, MyVias:Stitchging-Via-0.3-0.5, F.Cu at (121.6, 63.0)
- added REF**: Stitching-Via-0.3-0.5, MyVias:Stitchging-Via-0.3-0.5, F.Cu at (121.6, 65.0)
- added REF**: Stitching-Via-0.3-0.5, MyVias:Stitchging-Via-0.3-0.5, F.Cu at (114.0, 62.5)
- added REF**: Stitching-Via-0.3-0.5, MyVias:Stitchging-Via-0.3-0.5, F.Cu at (114.0, 65.0)
- added REF**: Stitching-Via-0.3-0.5, MyVias:Stitchging-Via-0.3-0.5, F.Cu at (106.6, 63.0)
- added REF**: Stitching-Via-0.3-0.5, MyVias:Stitchging-Via-0.3-0.5, F.Cu at (132.5, 128.0)
- added REF**: Stitching-Via-0.3-0.5, MyVias:Stitchging-Via-0.3-0.5, F.Cu at (106.6, 64.8)
- added REF**: Stitching-Via-0.3-0.5, MyVias:Stitchging-Via-0.3-0.5, F.Cu at (105.4, 64.8)
- added REF**: Stitching-Via-0.3-0.5, MyVias:Stitchging-Via-0.3-0.5, F.Cu at (100.8, 64.8)
- added REF**: Stitching-Via-0.3-0.5, MyVias:Stitchging-Via-0.3-0.5, F.Cu at (130.5, 128.0)
- added REF**: Stitching-Via-0.3-0.5, MyVias:Stitchging-Via-0.3-0.5, F.Cu at (161.0, 128.0)
- added REF**: Stitching-Via-0.3-0.5, MyVias:Stitchging-Via-0.3-0.5, F.Cu at (163.0, 128.0)
- added REF**: Stitching-Via-0.3-0.5, MyVias:Stitchging-Via-0.3-0.5, F.Cu at (119.1, 103.6)
- added REF**: Stitching-Via-0.3-0.5, MyVias:Stitchging-Via-0.3-0.5, F.Cu at (165.0, 128.0)
- added REF**: Stitching-Via-0.3-0.5, MyVias:Stitchging-Via-0.3-0.5, F.Cu at (166.8, 128.0)
- added REF**: Stitching-Via-0.3-0.5, MyVias:Stitchging-Via-0.3-0.5, F.Cu at (174.4, 128.0)
- added REF**: Stitching-Via-0.3-0.5, MyVias:Stitchging-Via-0.3-0.5, F.Cu at (172.7, 128.0)
- added REF**: Stitching-Via-0.3-0.5, MyVias:Stitchging-Via-0.3-0.5, F.Cu at (170.6, 128.0)
- added REF**: Stitching-Via-0.3-0.5, MyVias:Stitchging-Via-0.3-0.5, F.Cu at (168.6, 128.0)
- added REF**: Stitching-Via-0.3-0.5, MyVias:Stitchging-Via-0.3-0.5, F.Cu at (153.4, 128.0)
- added REF**: Stitching-Via-0.3-0.5, MyVias:Stitchging-Via-0.3-0.5, F.Cu at (155.4, 128.0)
- added REF**: Stitching-Via-0.3-0.5, MyVias:Stitchging-Via-0.3-0.5, F.Cu at (157.4, 128.0)
- added REF**: Stitching-Via-0.3-0.5, MyVias:Stitchging-Via-0.3-0.5, F.Cu at (159.2, 128.0)
- added REF**: Stitching-Via-0.3-0.5, MyVias:Stitchging-Via-0.3-0.5, F.Cu at (134.3, 103.6)
- added REF**: Stitching-Via-0.3-0.5, MyVias:Stitchging-Via-0.3-0.5, F.Cu at (151.6, 128.0)
- added REF**: Stitching-Via-0.3-0.5, MyVias:Stitchging-Via-0.3-0.5, F.Cu at (149.8, 128.0)
- added REF**: Stitching-Via-0.3-0.5, MyVias:Stitchging-Via-0.3-0.5, F.Cu at (147.8, 128.0)
- added REF**: Stitching-Via-0.3-0.5, MyVias:Stitchging-Via-0.3-0.5, F.Cu at (180.3, 128.0)
- added REF**: Stitching-Via-0.3-0.5, MyVias:Stitchging-Via-0.3-0.5, F.Cu at (178.3, 128.0)
- added REF**: Stitching-Via-0.3-0.5, MyVias:Stitchging-Via-0.3-0.5, F.Cu at (176.2, 128.0)
- added REF**: Stitching-Via-0.3-0.5, MyVias:Stitchging-Via-0.3-0.5, F.Cu at (142.2, 103.6)
- added REF**: Stitching-Via-0.3-0.5, MyVias:Stitchging-Via-0.3-0.5, F.Cu at (144.0, 103.6)
- added REF**: Stitching-Via-0.3-0.5, MyVias:Stitchging-Via-0.3-0.5, F.Cu at (163.0, 103.6)
- added REF**: Stitching-Via-0.3-0.5, MyVias:Stitchging-Via-0.3-0.5, F.Cu at (165.0, 103.6)
- added REF**: Stitching-Via-0.3-0.5, MyVias:Stitchging-Via-0.3-0.5, F.Cu at (136.3, 103.6)
- added REF**: Stitching-Via-0.3-0.5, MyVias:Stitchging-Via-0.3-0.5, F.Cu at (166.8, 103.6)
- added REF**: Stitching-Via-0.3-0.5, MyVias:Stitchging-Via-0.3-0.5, F.Cu at (174.4, 103.6)
- added REF**: Stitching-Via-0.3-0.5, MyVias:Stitchging-Via-0.3-0.5, F.Cu at (172.7, 103.6)
- added REF**: Stitching-Via-0.3-0.5, MyVias:Stitchging-Via-0.3-0.5, F.Cu at (170.6, 103.6)
- added REF**: Stitching-Via-0.3-0.5, MyVias:Stitchging-Via-0.3-0.5, F.Cu at (168.6, 103.6)
- added REF**: Stitching-Via-0.3-0.5, MyVias:Stitchging-Via-0.3-0.5, F.Cu at (155.4, 103.6)
- added REF**: Stitching-Via-0.3-0.5, MyVias:Stitchging-Via-0.3-0.5, F.Cu at (157.4, 103.6)
- added REF**: Stitching-Via-0.3-0.5, MyVias:Stitchging-Via-0.3-0.5, F.Cu at (159.2, 103.6)
- added REF**: Stitching-Via-0.3-0.5, MyVias:Stitchging-Via-0.3-0.5, F.Cu at (151.6, 103.6)
- added REF**: Stitching-Via-0.3-0.5, MyVias:Stitchging-Via-0.3-0.5, F.Cu at (149.8, 103.6)
- added REF**: Stitching-Via-0.3-0.5, MyVias:Stitchging-Via-0.3-0.5, F.Cu at (138.4, 103.6)
- added REF**: Stitching-Via-0.3-0.5, MyVias:Stitchging-Via-0.3-0.5, F.Cu at (147.8, 103.6)
- added REF**: Stitching-Via-0.3-0.5, MyVias:Stitchging-Via-0.3-0.5, F.Cu at (145.7, 103.6)
- added REF**: Stitching-Via-0.3-0.5, MyVias:Stitchging-Via-0.3-0.5, F.Cu at (155.7, 93.2)
- added REF**: Stitching-Via-0.3-0.5, MyVias:Stitchging-Via-0.3-0.5, F.Cu at (161.5, 93.2)
- added REF**: Stitching-Via-0.3-0.5, MyVias:Stitchging-Via-0.3-0.5, F.Cu at (163.3, 93.2)
- added REF**: Stitching-Via-0.3-0.5, MyVias:Stitchging-Via-0.3-0.5, F.Cu at (174.7, 93.3)
- added REF**: Stitching-Via-0.3-0.5, MyVias:Stitchging-Via-0.3-0.5, F.Cu at (140.4, 93.2)
- added REF**: Stitching-Via-0.3-0.5, MyVias:Stitchging-Via-0.3-0.5, F.Cu at (142.4, 93.2)
- added REF**: Stitching-Via-0.3-0.5, MyVias:Stitchging-Via-0.3-0.5, F.Cu at (144.5, 93.2)
- added REF**: Stitching-Via-0.3-0.5, MyVias:Stitchging-Via-0.3-0.5, F.Cu at (146.3, 93.2)
- added REF**: Stitching-Via-0.3-0.5, MyVias:Stitchging-Via-0.3-0.5, F.Cu at (132.5, 103.6)
- added REF**: Stitching-Via-0.3-0.5, MyVias:Stitchging-Via-0.3-0.5, F.Cu at (152.1, 93.2)
- added REF**: Stitching-Via-0.3-0.5, MyVias:Stitchging-Via-0.3-0.5, F.Cu at (150.1, 93.2)
- added REF**: Stitching-Via-0.3-0.5, MyVias:Stitchging-Via-0.3-0.5, F.Cu at (148.0, 93.2)
- added REF**: Stitching-Via-0.3-0.5, MyVias:Stitchging-Via-0.3-0.5, F.Cu at (132.8, 93.2)
- added REF**: Stitching-Via-0.3-0.5, MyVias:Stitchging-Via-0.3-0.5, F.Cu at (134.8, 93.2)
- added REF**: Stitching-Via-0.3-0.5, MyVias:Stitchging-Via-0.3-0.5, F.Cu at (138.6, 93.2)
- added REF**: Stitching-Via-0.3-0.5, MyVias:Stitchging-Via-0.3-0.5, F.Cu at (131.0, 93.2)
- added REF**: Stitching-Via-0.3-0.5, MyVias:Stitchging-Via-0.3-0.5, F.Cu at (127.2, 93.2)
- added REF**: Stitching-Via-0.3-0.5, MyVias:Stitchging-Via-0.3-0.5, F.Cu at (125.2, 93.2)
- added REF**: Stitching-Via-0.3-0.5, MyVias:Stitchging-Via-0.3-0.5, F.Cu at (165.8, 74.2)
- added REF**: Stitching-Via-0.3-0.5, MyVias:Stitchging-Via-0.3-0.5, F.Cu at (130.8, 103.6)
- added REF**: Stitching-Via-0.3-0.5, MyVias:Stitchging-Via-0.3-0.5, F.Cu at (165.8, 75.9)
- added REF**: Stitching-Via-0.3-0.5, MyVias:Stitchging-Via-0.3-0.5, F.Cu at (158.2, 73.9)
- added REF**: Stitching-Via-0.3-0.5, MyVias:Stitchging-Via-0.3-0.5, F.Cu at (158.2, 75.9)
- added REF**: Stitching-Via-0.3-0.5, MyVias:Stitchging-Via-0.3-0.5, F.Cu at (150.3, 75.9)
- added REF**: Stitching-Via-0.3-0.5, MyVias:Stitchging-Via-0.3-0.5, F.Cu at (135.6, 75.9)
- added REF**: Stitching-Via-0.3-0.5, MyVias:Stitchging-Via-0.3-0.5, F.Cu at (143.0, 75.9)
- added REF**: Stitching-Via-0.3-0.5, MyVias:Stitchging-Via-0.3-0.5, F.Cu at (128.2, 75.9)
- added REF**: Stitching-Via-0.3-0.5, MyVias:Stitchging-Via-0.3-0.5, F.Cu at (121.6, 75.9)
- added REF**: Stitching-Via-0.3-0.5, MyVias:Stitchging-Via-0.3-0.5, F.Cu at (121.6, 73.9)
- added REF**: Stitching-Via-0.3-0.5, MyVias:Stitchging-Via-0.3-0.5, F.Cu at (114.2, 75.9)
- added REF**: Stitching-Via-0.3-0.5, MyVias:Stitchging-Via-0.3-0.5, F.Cu at (126.7, 103.6)
- added REF**: Stitching-Via-0.3-0.5, MyVias:Stitchging-Via-0.3-0.5, F.Cu at (114.2, 73.9)
- added REF**: Stitching-Via-0.3-0.5, MyVias:Stitchging-Via-0.3-0.5, F.Cu at (106.6, 75.9)
- added REF**: Stitching-Via-0.3-0.5, MyVias:Stitchging-Via-0.3-0.5, F.Cu at (106.6, 73.9)
- added REF**: Stitching-Via-0.3-0.5, MyVias:Stitchging-Via-0.3-0.5, F.Cu at (148.9, 111.4)
- added REF**: Stitching-Via-0.3-0.5, MyVias:Stitchging-Via-0.3-0.5, F.Cu at (164.3, 120.7)
- added REF**: Stitching-Via-0.3-0.5, MyVias:Stitchging-Via-0.3-0.5, F.Cu at (164.3, 121.7)
- added REF**: Stitching-Via-0.3-0.5, MyVias:Stitchging-Via-0.3-0.5, F.Cu at (164.3, 122.7)
- added REF**: Stitching-Via-0.3-0.5, MyVias:Stitchging-Via-0.3-0.5, F.Cu at (164.3, 116.6)
- added REF**: Stitching-Via-0.3-0.5, MyVias:Stitchging-Via-0.3-0.5, F.Cu at (164.3, 115.6)
- added REF**: Stitching-Via-0.3-0.5, MyVias:Stitchging-Via-0.3-0.5, F.Cu at (164.3, 112.5)
- added REF**: Stitching-Via-0.3-0.5, MyVias:Stitchging-Via-0.3-0.5, F.Cu at (117.3, 128.0)
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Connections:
- U1 pad 17: (no net) -> GND
- U10 pad 17: (no net) -> GND
- U11 pad 17: (no net) -> GND
- U12 pad 17: (no net) -> GND
- U13 pad 17: (no net) -> GND
- U14 pad 17: (no net) -> GND
- U15 pad 17: (no net) -> GND
- U16 pad 17: (no net) -> GND
- U17 pad 17: (no net) -> GND
- U18 pad 17: (no net) -> GND
- U19 pad 17: (no net) -> GND
- U2 pad 17: (no net) -> GND
- U20 pad 17: (no net) -> GND
- U21 pad 17: (no net) -> GND
- U22 pad 17: (no net) -> GND
- U23 pad 17: (no net) -> GND
- U24 pad 17: (no net) -> GND
- U25 pad 17: (no net) -> GND
- U26 pad 17: (no net) -> GND
- U27 pad 17: (no net) -> GND
- U28 pad 17: (no net) -> GND
- U29 pad 17: (no net) -> GND
- U3 pad 17: (no net) -> GND
- U30 pad 17: (no net) -> GND
- U31 pad 17: (no net) -> GND
- U32 pad 17: (no net) -> GND
- U34 pad 17: (no net) -> GND
- U4 pad 17: (no net) -> GND
- U5 pad 17: (no net) -> GND
- U6 pad 17: (no net) -> GND
- U7 pad 17: (no net) -> GND
- U8 pad 17: (no net) -> GND
- U9 pad 17: (no net) -> GND
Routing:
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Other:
- board text added: "64 LED Driver Stages"
- board text added: "< I2C"
- board text added: "DAC"
- board text added: "OFF"
- board text added: "POTI"
- board text added: "Power Supply"
- board text added: "SPI >"
- board text added: "max. 200 mA / transistor"
- board text added: "max. 3.36 A 24 V"
- board text added: "max. 350 mW dissipation / transistor"
- board text removed: "max. 3.36 A 26 V"
